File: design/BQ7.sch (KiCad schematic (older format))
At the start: 45 parts

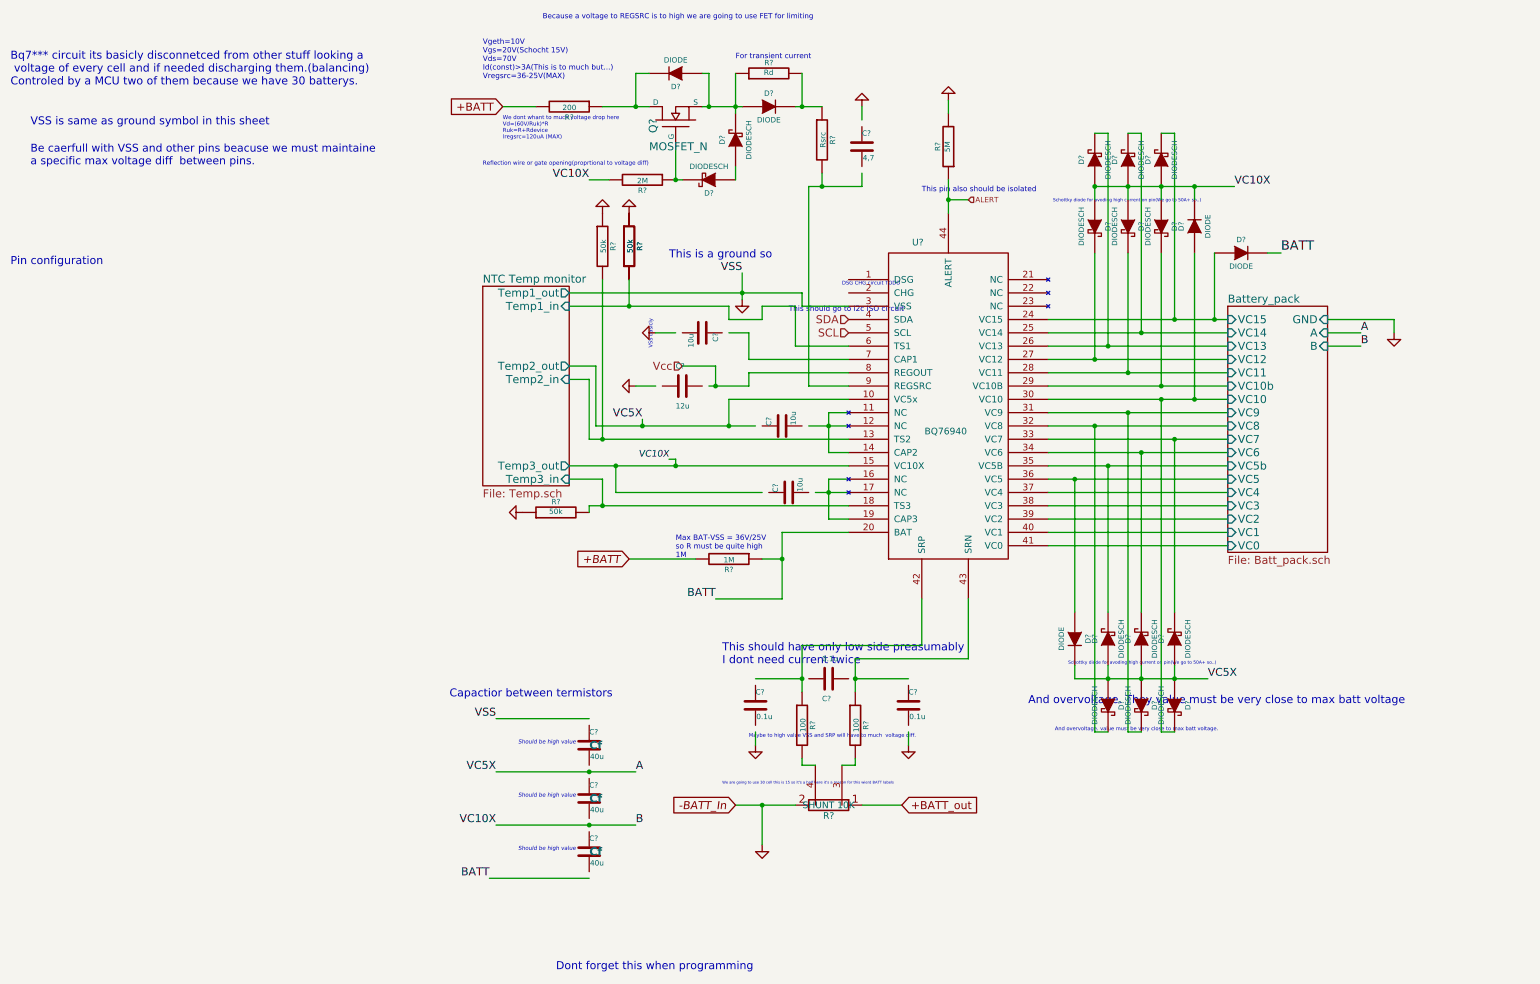
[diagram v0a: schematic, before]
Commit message: Fix some schematic update pdf
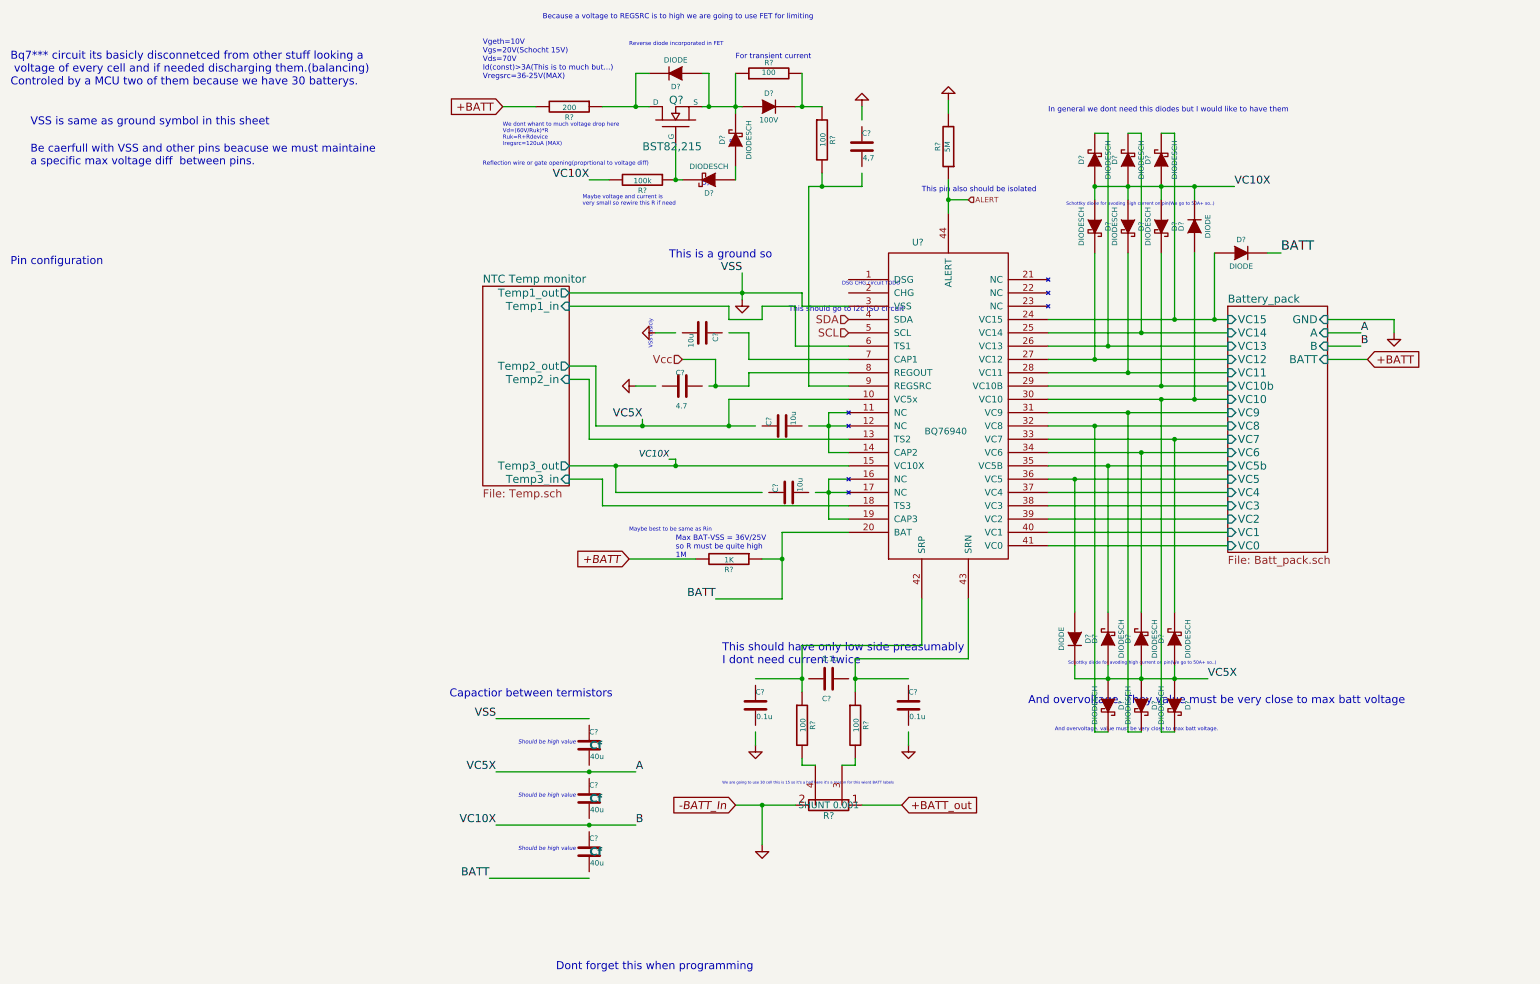
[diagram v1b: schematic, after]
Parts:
- removed R? (x4): 50k, symbol R
- C?: value 12u -> 4.7
- D?: value DIODE -> 100V
- Q?: value MOSFET_N -> BST82,215
- R?: value SHUNT 10K -> SHUNT 0.001
- R?: value 2M -> 100k
- R?: value 1M -> 1K
- R?: value Rd -> 100
- R?: value Rsrc -> 100
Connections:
- wire segments 152 -> 150
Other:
- note added: "5,2"
- note added: "In general we dont need this diodes but I would like to have them"
- note added: "Maybe best to be same as Rin"
- note added: "Maybe voltage and current is \nvery small so rewire this R if need"
- note added: "Reverse diode incorporated in FET"
- note removed: "Maybe to high value VSS and SRP will have to much voltage diff.\n"
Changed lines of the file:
@@
 00 00 00 00 00 00 00 00 00 00 00 00 00 00 00 00 00 00 00 00 00 00 00 00 00 00 00 00 00 00 00 00
 00 00 00 00 00 00 00 00 00 00 00 28 F5 FF 00 A1 2A 35 C4 84 81 83 FF 00 00 00 00 49 45 4E 44 AE
-42 60 82 00
+42 60 82 09
 EndData
 $EndBitmap
@@
 9F DF D1 D1 31 D6 A5 40 90 E1 4D 94 96 C0 77 F7 E1 9C E9 BB 40 B5 84 6A 00 41 90 F1 06 B5 8D 23
 08 82 20 C8 04 83 62 36 82 20 08 82 4C 0C 38 D4 12 88 20 08 82 20 E3 1C 1A 1D 89 20 08 82 20 08
-82 20 08 82 20 23 ED FF 01 11 4E 07 64 6B 3C CF 2D 00 00 00 00 49 45 4E 44 AE 42 60 82 6A
+82 20 08 82 20 23 ED FF 01 11 4E 07 64 6B 3C CF 2D 00 00 00 00 49 45 4E 44 AE 42 60 82 33
 EndData
 $EndBitmap
@@
 	-1   0    0    1
 $EndComp
-$Comp
-L R R?
-U 1 1 558480EE
-P 5300 2050
-F 0 "R?" V 5380 2050 40  0000 C CNN
-F 1 "50k" V 5307 2051 40  0000 C CNN
-F 2 "" V 5230 2050 30  0000 C CNN
-F 3 "" H 5300 2050 30  0000 C CNN
-	1    5300 2050
-	1    0    0    -1
-$EndComp
-$Comp
-L R R?
-U 1 1 55848215
-P 5100 2050
-F 0 "R?" V 5180 2050 40  0000 C CNN
-F 1 "50k" V 5107 2051 40  0000 C CNN
-F 2 "" V 5030 2050 30  0000 C CNN
-F 3 "" H 5100 2050 30  0000 C CNN
-	1    5100 2050
-	1    0    0    -1
-$EndComp
-$Comp
-L R R?
-U 1 1 5584841E
-P 4750 4050
-F 0 "R?" V 4830 4050 40  0000 C CNN
-F 1 "50k" V 4757 4051 40  0000 C CNN
-F 2 "" V 4680 4050 30  0000 C CNN
-F 3 "" H 4750 4050 30  0000 C CNN
-	1    4750 4050
-	0    -1   -1   0
-$EndComp
-$Comp
-L GND #PWR06
-U 1 1 55848488
-P 5300 1800
-F 0 "#PWR06" H 5300 1800 30  0001 C CNN
-F 1 "GND" H 5300 1730 30  0001 C CNN
-F 2 "" H 5300 1800 60  0000 C CNN
-F 3 "" H 5300 1800 60  0000 C CNN
-	1    5300 1800
-	-1   0    0    1
-$EndComp
-$Comp
-L GND #PWR07
-U 1 1 5584850F
-P 5100 1800
-F 0 "#PWR07" H 5100 1800 30  0001 C CNN
-F 1 "GND" H 5100 1730 30  0001 C CNN
-F 2 "" H 5100 1800 60  0000 C CNN
-F 3 "" H 5100 1800 60  0000 C CNN
-	1    5100 1800
-	-1   0    0    1
-$EndComp
-$Comp
-L GND #PWR08
-U 1 1 558485AD
-P 4500 4050
-F 0 "#PWR08" H 4500 4050 30  0001 C CNN
-F 1 "GND" H 4500 3980 30  0001 C CNN
-F 2 "" H 4500 4050 60  0000 C CNN
-F 3 "" H 4500 4050 60  0000 C CNN
-	1    4500 4050
-	0    1    1    0
-$EndComp
 Text GLabel 7350 6250 2    60   Input ~ 0
 +BATT_out
@@
 P 6800 6250
 F 0 "R?" V 6880 6250 50  0000 C CNN
-F 1 "SHUNT 10K" V 6800 6250 50  0000 C CNN
+F 1 "SHUNT 0.001" V 6800 6250 50  0000 C CNN
 F 2 "" H 6800 6250 60  0000 C CNN
 F 3 "" H 6800 6250 60  0000 C CNN
@@
 P 6050 4400
 F 0 "R?" V 6130 4400 40  0000 C CNN
-F 1 "1M" V 6057 4401 40  0000 C CNN
+F 1 "1K" V 6057 4401 40  0000 C CNN
 F 2 "" V 5980 4400 30  0000 C CNN
 F 3 "" H 6050 4400 30  0000 C CNN
@@
 P 5400 1550
 F 0 "R?" V 5480 1550 40  0000 C CNN
-F 1 "2M" V 5407 1551 40  0000 C CNN
+F 1 "100k" V 5407 1551 40  0000 C CNN
 F 2 "" V 5330 1550 30  0000 C CNN
 F 3 "" H 5400 1550 30  0000 C CNN
@@
 U 1 1 55BCC7C1
 P 5650 1100
-F 0 "Q?" H 5660 1270 60  0000 R CNN
-F 1 "MOSFET_N" V 5450 1300 60  0000 R CNN
+F 0 "Q?" V 5800 1150 60  0000 R CNN
+F 1 "BST82,215" V 5450 1350 60  0000 R CNN
 F 2 "" H 5650 1100 60  0000 C CNN
 F 3 "" H 5650 1100 60  0000 C CNN
@@
 P 6350 1000
 F 0 "D?" H 6350 1100 40  0000 C CNN
-F 1 "DIODE" H 6350 900 40  0000 C CNN
+F 1 "100V" H 6350 900 40  0000 C CNN
 F 2 "" H 6350 1000 60  0000 C CNN
 F 3 "" H 6350 1000 60  0000 C CNN
@@
 P 6350 750
 F 0 "R?" V 6430 750 40  0000 C CNN
-F 1 "Rd" V 6357 751 40  0000 C CNN
+F 1 "100" V 6357 751 40  0000 C CNN
 F 2 "" V 6280 750 30  0000 C CNN
 F 3 "" H 6350 750 30  0000 C CNN
@@
 P 6750 1250
 F 0 "R?" V 6830 1250 40  0000 C CNN
-F 1 "Rsrc" V 6757 1251 40  0000 C CNN
+F 1 "100" V 6757 1251 40  0000 C CNN
 F 2 "" V 6680 1250 30  0000 C CNN
 F 3 "" H 6750 1250 30  0000 C CNN
@@
 U 1 1 55BCD3D7
 P 5700 3100
-F 0 "C?" V 5550 3050 40  0000 L CNN
-F 1 "12u" V 5850 3050 40  0000 L CNN
+F 0 "C?" V 5600 3050 40  0000 L CNN
+F 1 "4.7" V 5850 3050 40  0000 L CNN
 F 2 "" H 5738 2950 30  0000 C CNN
 F 3 "" H 5700 3100 60  0000 C CNN
@@
 	0    1    1    0
 $EndComp
-Text HLabel 5700 2950 0    60   Input ~ 0
+Text HLabel 5700 2900 0    60   Input ~ 0
 Vcc
 Text Notes 5650 4400 0    40   ~ 0
@@
 	0    -1   -1   0
 $EndComp
-Text Notes 9600 1724 2    24   ~ 0
+Text Notes 9700 1750 2    24   ~ 0
 Schottky diode for avoding high current on pin(We go to 50A+ so..)
 $Sheet
@@
 F21 "VC14" I L 9800 2700 60
 F22 "VC15" I L 9800 2600 60
+F23 "BATT" I R 10550 2900 60
 $EndSheet
 Text Label 10800 2700 0    60   ~ 0
@@
 Text Notes 8500 5700 0    28   ~ 0
 And overvoltage. value must be very close to max batt voltage.
-Text Notes 6200 5750 0    28   ~ 0
-Maybe to high value VSS and SRP will have to much  voltage diff.\n
 Text Notes 800  1450 0    59   ~ 0
 Be caerfull with VSS and other pins beacuse we must maintaine \na specific max voltage diff  between pins.\n
@@
 This should go to i2c ISO circuit
 $Comp
-L R R?
-U 1 1 55DBFB03
-P 5300 2050
-F 0 "R?" V 5380 2050 40  0000 C CNN
-F 1 "50k" V 5307 2051 40  0000 C CNN
-F 2 "" V 5230 2050 30  0000 C CNN
-F 3 "" H 5300 2050 30  0000 C CNN
-	1    5300 2050
-	1    0    0    -1
-$EndComp
-$Comp
 L C C?
 U 1 1 55DC3CEE
@@
 Text Notes 7500 1650 0    40   ~ 0
 This pin also should be isolated
-Text Label 10200 2100 0    70   ~ 0
-BATT
-$Comp
-L DIODE D?
-U 1 1 55DE2295
-P 9900 2100
-F 0 "D?" H 9900 2200 40  0000 C CNN
-F 1 "DIODE" H 9900 2000 40  0000 C CNN
-F 2 "" H 9900 2100 60  0000 C CNN
-F 3 "" H 9900 2100 60  0000 C CNN
-	1    9900 2100
-	1    0    0    -1
-$EndComp
 Text Notes 4200 800  0    40   ~ 0
 Vgeth=10V\nVgs=20V(Schocht 15V)\nVds=70V\nId(const)>3A(This is to much but...)\nVregsrc=36-25V(MAX)
+Text Notes 4350 1350 0    30   ~ 0
+We dont whant to much voltage drop here\nVd=(60V/Ruk)*R\nRuk=R+Rdevice\nIregsrc=120uA (MAX)\n		\n
+Text Notes 6100 650  0    40   ~ 0
+For transient current
+Text Notes 5850 1600 0    40   ~ 0
+5,2
+Text Notes 6050 1300 0    40   ~ 0
+5,2
+Text Notes 5300 550  0    30   ~ 0
+Reverse diode incorporated in FET
+Text Notes 8450 1050 0    40   ~ 0
+In general we dont need this diodes but I would like to have them
 Wire Wire Line
 	7700 1050 7700 950
@@
 	5350 3100 5500 3100
 Wire Wire Line
-	5700 2950 5950 2950
+	5700 2900 5950 2900
 Wire Wire Line
-	5950 2950 5950 3100
+	5950 2900 5950 3100
 Connection ~ 5950 3100
 Wire Wire Line
@@
 	6200 2700 6050 2700
 Wire Wire Line
-	5100 2300 5100 3500
-Connection ~ 5100 3500
-Wire Wire Line
-	5300 2300 5300 2500
-Connection ~ 5300 2500
-Wire Wire Line
 	5600 3650 5650 3650
 Wire Wire Line
@@
 Connection ~ 5650 3700
 Wire Wire Line
-	5000 4000 6950 4000
-Wire Wire Line
-	5000 4050 5000 4000
-Connection ~ 5100 4000
-Wire Wire Line
 	7700 1700 7850 1700
 Connection ~ 7700 1700
 Wire Wire Line
-	10100 2100 10200 2100
-Wire Wire Line
-	9700 2100 9700 2600
-Connection ~ 9700 2600
-Wire Wire Line
 	5450 750  5350 750
 Wire Wire Line
 	5350 750  5350 1000
 Connection ~ 5350 1000
-Text Notes 4350 1300 0    30   ~ 0
-We dont whant to much voltage drop here\nVd=(60V/Ruk)*R\nRuk=R+Rdevice\nIregsrc=120uA (MAX)\n		\n
-Text Notes 6100 650  0    40   ~ 0
-For transient current
+Wire Wire Line
+	5100 4000 6950 4000
+Connection ~ 9700 2600
+Wire Wire Line
+	9700 2100 9700 2600
+Wire Wire Line
+	10100 2100 10200 2100
+$Comp
+L DIODE D?
+U 1 1 55DE2295
+P 9900 2100
+F 0 "D?" H 9900 2200 40  0000 C CNN
+F 1 "DIODE" H 9900 2000 40  0000 C CNN
+F 2 "" H 9900 2100 60  0000 C CNN
+F 3 "" H 9900 2100 60  0000 C CNN
+	1    9900 2100
+	1    0    0    -1
+$EndComp
+Text Label 10200 2100 0    70   ~ 0
+BATT
+Text Notes 5300 4200 0    30   ~ 0
+Maybe best to be same as Rin
+Text GLabel 10850 2900 2    60   Input ~ 0
++BATT
+Wire Wire Line
+	10550 2900 10850 2900
+Text Notes 4950 1750 0    30   ~ 0
+Maybe voltage and current is \nvery small so rewire this R if need
 $EndSCHEMATC

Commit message: Fix some mistakes and some explanations
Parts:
- R?: value 100 -> 100K
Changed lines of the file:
@@
 P 6350 750
 F 0 "R?" V 6430 750 40  0000 C CNN
-F 1 "100" V 6357 751 40  0000 C CNN
+F 1 "100K" V 6357 751 40  0000 C CNN
 F 2 "" V 6280 750 30  0000 C CNN
 F 3 "" H 6350 750 30  0000 C CNN

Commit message: MCU datasheet
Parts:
- removed D? (x2): DIODESCH, symbol DIODESCH
- added D? (x2): ZENER, symbol ZENER
- R?: value 5M -> 300K

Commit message: Add a new BQ and start routing board for (reason for separation for easier routing) but in the end I souldnt do this becasue of netlist but its ok because of symlink
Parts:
- removed D? (x2): DIODE, symbol DIODE
- added D? (x2): DIODE, symbol DIODE
- C? (x8): symbol C -> C-RESCUE-BMS
- C? (x3): value 10u -> 1u; symbol C -> C-RESCUE-BMS
- D?: Value (none) -> 100V
- D? (x2): symbol ZENER -> ZENER-RESCUE-BMS
- R? (x8): symbol R -> R-RESCUE-BMS
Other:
- note added: "0,8 value of Schotcky"
- note added: "Gate value\n"
- note added: "Max BAT-VSS = 36V/25V\nso R must be quite high \n1K\n"
- note removed: "Max BAT-VSS = 36V/25V\nso R must be quite high \n1M"
